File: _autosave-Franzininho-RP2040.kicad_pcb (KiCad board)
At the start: 2 copper layers, 37 parts, among them J1 USB_B_Micro, J2 Conn_01x02, J3 Conn_01x04, J4 Conn_01x17, J5 Conn_01x17, SW1 SW_Push, U1 RP2040, U2 NCP1117-3.3_SOT223, U3 W25Q128JVS, Y1 12MHz

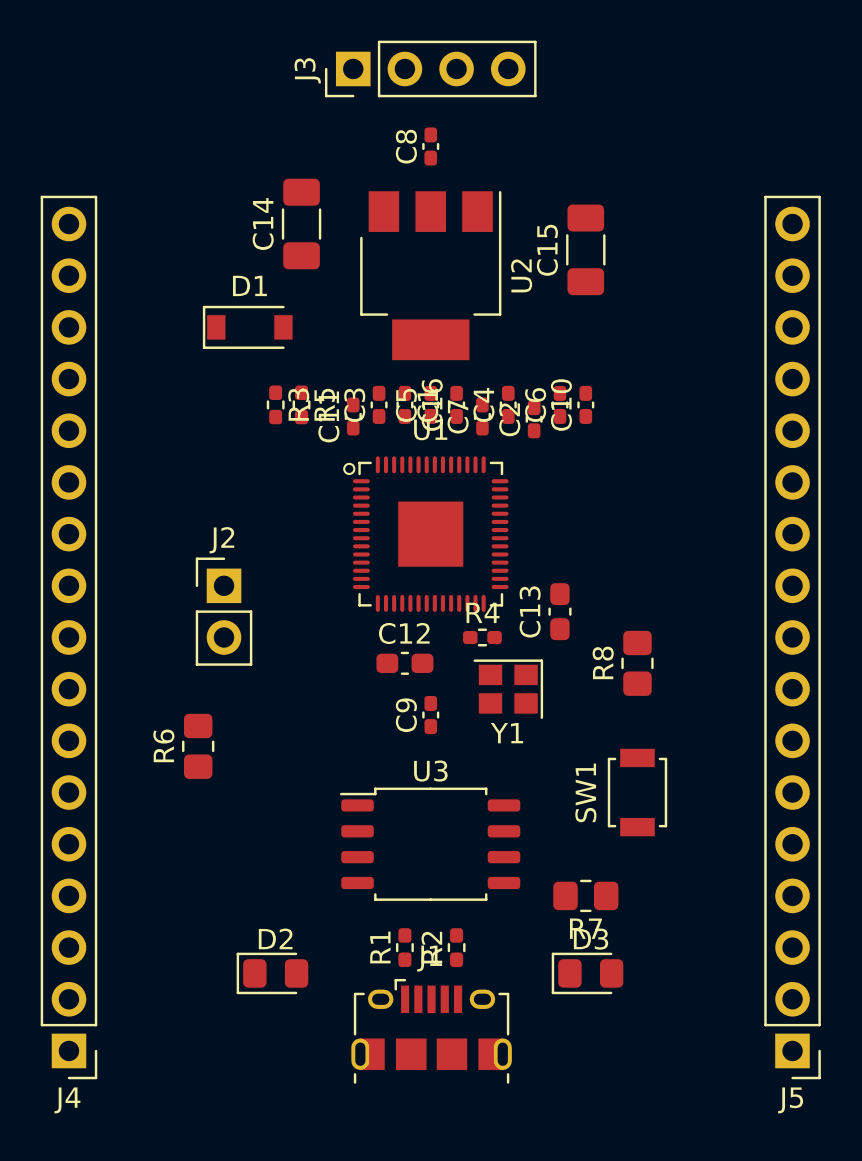
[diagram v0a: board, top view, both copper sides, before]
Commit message: Geração de netlist e posicionamento inicial de componentes na PCB
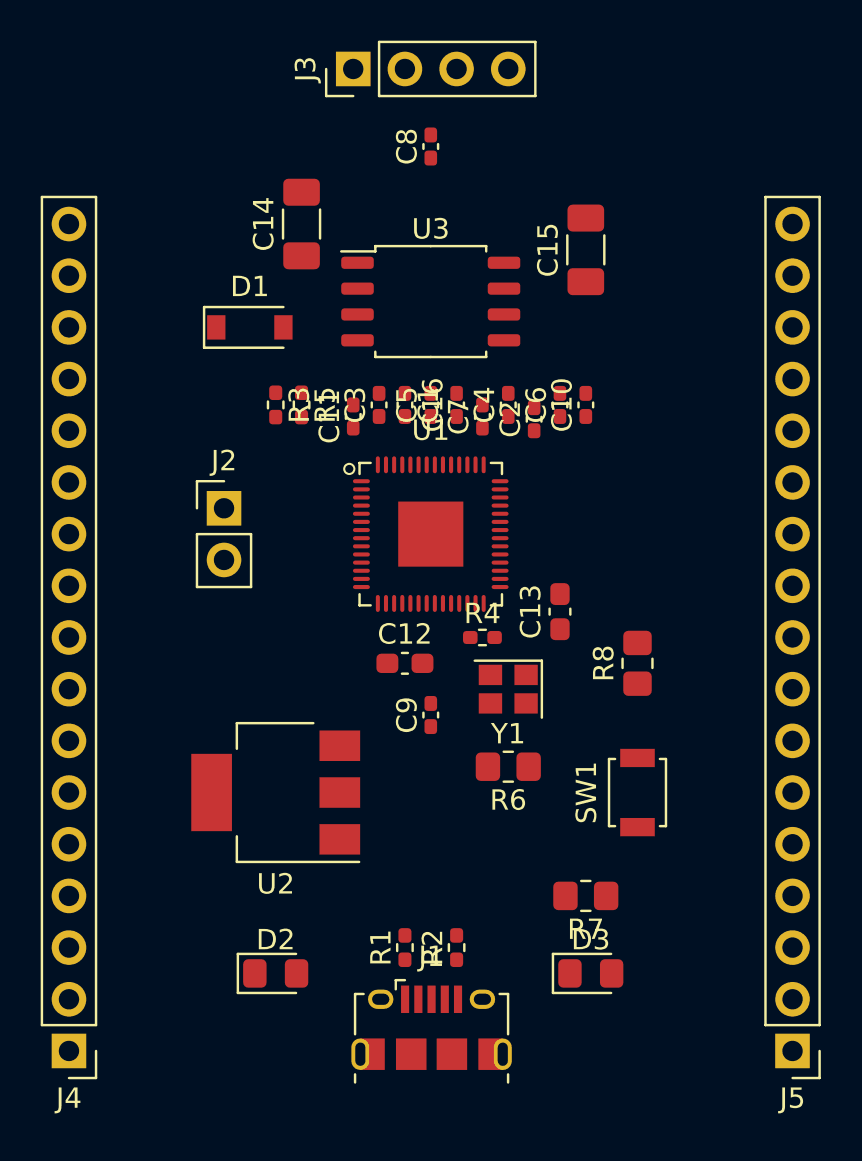
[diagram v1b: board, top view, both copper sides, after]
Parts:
- moved U3 26.7 mm to (104.1, -43.2)
- moved U2 26.5 mm to (96.5, -19.1), turned to 180 degrees
- moved R6 15.3 mm to (108.0, -20.3), turned to 180 degrees
- moved J2 3.81 mm to (94.0, -33.0)
